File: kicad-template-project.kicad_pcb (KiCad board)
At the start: 4 copper layers, 1 part

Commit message: feat: initial layout
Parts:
- added C10: C, Capacitor_SMD:C_1206_3216Metric, B.Cu at (120.5, 145.0)
- added C11: C, Capacitor_SMD:C_1206_3216Metric, B.Cu at (118.0, 145.0)
- added C12: C, Capacitor_SMD:C_1206_3216Metric, B.Cu at (115.5, 145.0)
- added C13: C, Capacitor_SMD:C_1206_3216Metric, B.Cu at (132.5, 145.0)
- added C14: C, Capacitor_SMD:C_1206_3216Metric, B.Cu at (130.0, 145.0)
- added C15: C, Capacitor_SMD:C_1206_3216Metric, B.Cu at (127.5, 145.0)
- added C16: C, Capacitor_SMD:C_1206_3216Metric, B.Cu at (142.0, 145.0)
- added C19: C, Capacitor_SMD:C_1206_3216Metric, B.Cu at (139.5, 145.0)
- added C2: 100 nF, chenry-footprint-lib:C_0402, F.Cu at (141.0, 152.7)
- added C26: 100 nF, chenry-footprint-lib:C_0402, F.Cu at (117.0, 152.7)
- added C27: 100 nF, chenry-footprint-lib:C_0402, F.Cu at (129.0, 152.7)
- added C29: 100 nF, chenry-footprint-lib:C_0402, B.Cu at (117.8, 149.5)
- added C3: 100 nF, chenry-footprint-lib:C_0402, F.Cu at (122.0, 146.0)
- added C30: 100 nF, chenry-footprint-lib:C_0402, B.Cu at (129.8, 149.5)
- added C31: 100 nF, chenry-footprint-lib:C_0402, B.Cu at (141.8, 149.5)
- added C32: 100 nF, chenry-footprint-lib:C_0402, B.Cu at (116.8, 149.5)
- added C33: 100 nF, chenry-footprint-lib:C_0402, B.Cu at (128.8, 149.5)
- added C34: 100 nF, chenry-footprint-lib:C_0402, B.Cu at (140.8, 149.5)
- added C35: 100 nF, chenry-footprint-lib:C_0402, B.Cu at (115.8, 149.5)
- added C36: 100 nF, chenry-footprint-lib:C_0402, B.Cu at (127.8, 149.5)
- added C37: 100 nF, chenry-footprint-lib:C_0402, B.Cu at (139.8, 149.5)
- added C38: C, Capacitor_SMD:C_1206_3216Metric, B.Cu at (113.0, 145.0)
- added C39: C, Capacitor_SMD:C_1206_3216Metric, B.Cu at (125.0, 145.0)
- added C4: 100 nF, chenry-footprint-lib:C_0402, F.Cu at (113.5, 151.5)
- added C5: 100 nF, chenry-footprint-lib:C_0402, F.Cu at (134.0, 146.0)
- added C6: 100 nF, chenry-footprint-lib:C_0402, F.Cu at (125.5, 151.5)
- added C7: 100 nF, chenry-footprint-lib:C_0402, F.Cu at (137.5, 151.5)
- added C8: C, Capacitor_SMD:C_1206_3216Metric, B.Cu at (137.0, 145.0)
- added C9: C, Capacitor_SMD:C_1206_3216Metric, B.Cu at (144.5, 145.0)
- added H1: MountingHole_Pad, MountingHole:MountingHole_2.2mm_M2_DIN965_Pad, F.Cu at (138.0, 156.0)
- added H2: MountingHole_Pad, MountingHole:MountingHole_2.2mm_M2_DIN965_Pad, F.Cu at (120.5, 155.5)
- added H3: MountingHole_Pad, MountingHole:MountingHole_2.2mm_M2_DIN965_Pad, F.Cu at (129.0, 157.5)
- added J1: Conn_01x02_Pin, Connector_AMASS:AMASS_XT30PW-F_1x02_P2.50mm_Horizontal, F.Cu at (147.1, 132.8)
- added Q1: LMG2100R026, chenry-footprint-lib:VBN0018A-MFG, F.Cu at (140.5, 148.5)
- added Q2: LMG2100R026, chenry-footprint-lib:VBN0018A-MFG, F.Cu at (116.5, 148.5)
- added Q3: LMG2100R026, chenry-footprint-lib:VBN0018A-MFG, F.Cu at (128.5, 148.5)
- added R1: 10K, chenry-footprint-lib:R_0402, F.Cu at (147.0, 152.0)
- added R2: 10K, chenry-footprint-lib:R_0402, F.Cu at (123.0, 152.0)
- added R3: 10K, chenry-footprint-lib:R_0402, F.Cu at (135.0, 152.0)
- added U1: MCS1823, chenry-footprint-lib:MPS_MCS1823_TQFN-12_MNP, F.Cu at (145.8, 149.2)
- added U2: MCS1823, chenry-footprint-lib:MPS_MCS1823_TQFN-12_MNP, F.Cu at (121.8, 149.2)
- added U3: MCS1823, chenry-footprint-lib:MPS_MCS1823_TQFN-12_MNP, F.Cu at (133.8, 149.2)
- added U4: ICE40UP5K-SG48ITR, Package_DFN_QFN:QFN-48-1EP_7x7mm_P0.5mm_EP5.6x5.6mm, F.Cu at (112.0, 130.2)
- added U5: STM32G0B1RETx, Package_QFP:LQFP-64_10x10mm_P0.5mm, F.Cu at (121.8, 121.0)
- added U6: SN65HVD230, Package_SO:SOIC-8_3.9x4.9mm_P1.27mm, F.Cu at (133.8, 115.2)
- added U7: LAN8710A, Package_DFN_QFN:QFN-32-1EP_5x5mm_P0.5mm_EP3.3x3.3mm_ThermalVias, F.Cu at (133.8, 122.8)
- added U8: MLX90395xLW, Package_DFN_QFN:QFN-16-1EP_3x3mm_P0.5mm_EP1.675x1.675mm, B.Cu at (130.0, 135.0)
- C1: value 1 uF -> 100 nF
- moved C1 46.1 mm to (146.0, 146.0), turned to -90 degrees
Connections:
- C1 pad 1: unconnected-(C1-Pad1) -> GND
- C1 pad 2: unconnected-(C1-Pad2) -> VDD_3V3
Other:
- board outline added: 50 x 50 mm

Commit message: fix: adjusted positining
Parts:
- added U10: AD40xxBCPZ, Package_CSP:LFCSP-WD-10-1EP_3x3mm_P0.5mm_EP1.64x2.38mm, F.Cu at (128.8, 140.5)
- added U11: AD40xxBCPZ, Package_CSP:LFCSP-WD-10-1EP_3x3mm_P0.5mm_EP1.64x2.38mm, F.Cu at (140.5, 140.5)
- added U9: AD40xxBCPZ, Package_CSP:LFCSP-WD-10-1EP_3x3mm_P0.5mm_EP1.64x2.38mm, F.Cu at (116.8, 140.2)
- moved U4 1.00 mm to (112.0, 131.2)

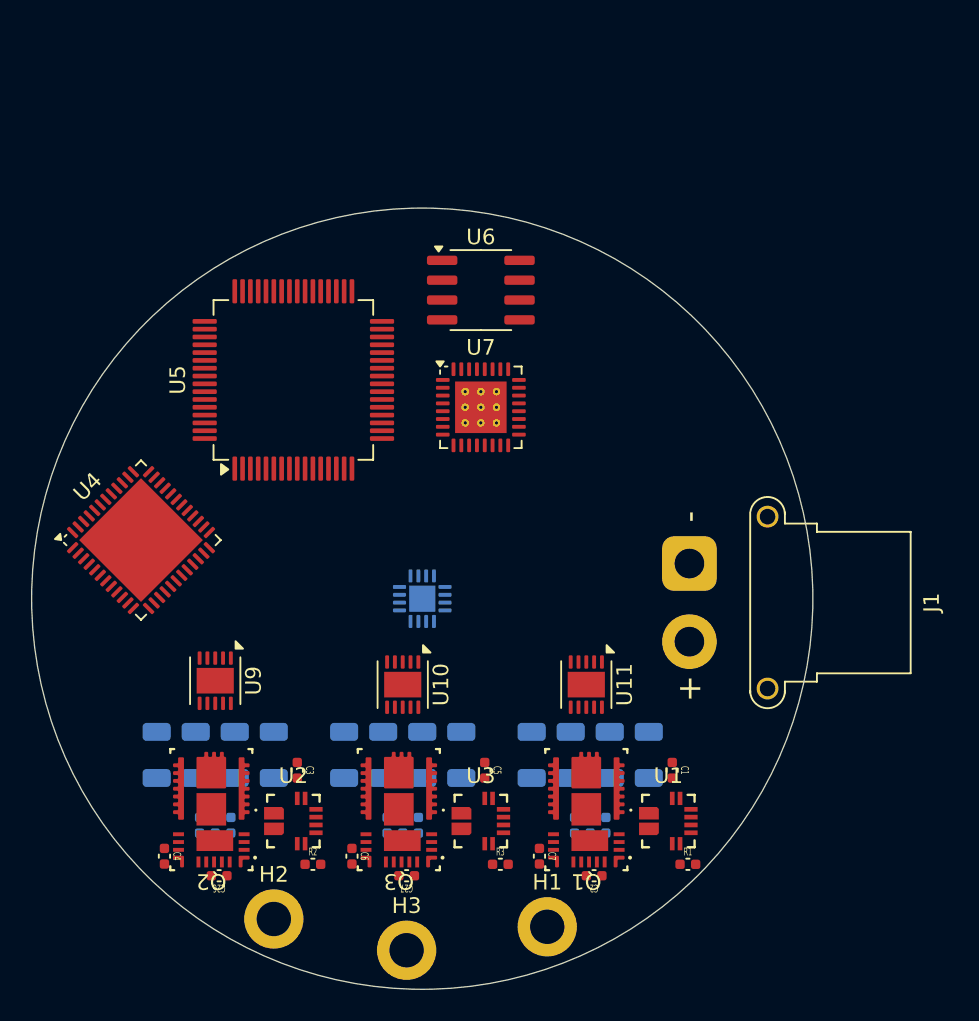
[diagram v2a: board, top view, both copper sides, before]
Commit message: fix: added switcher placeholders
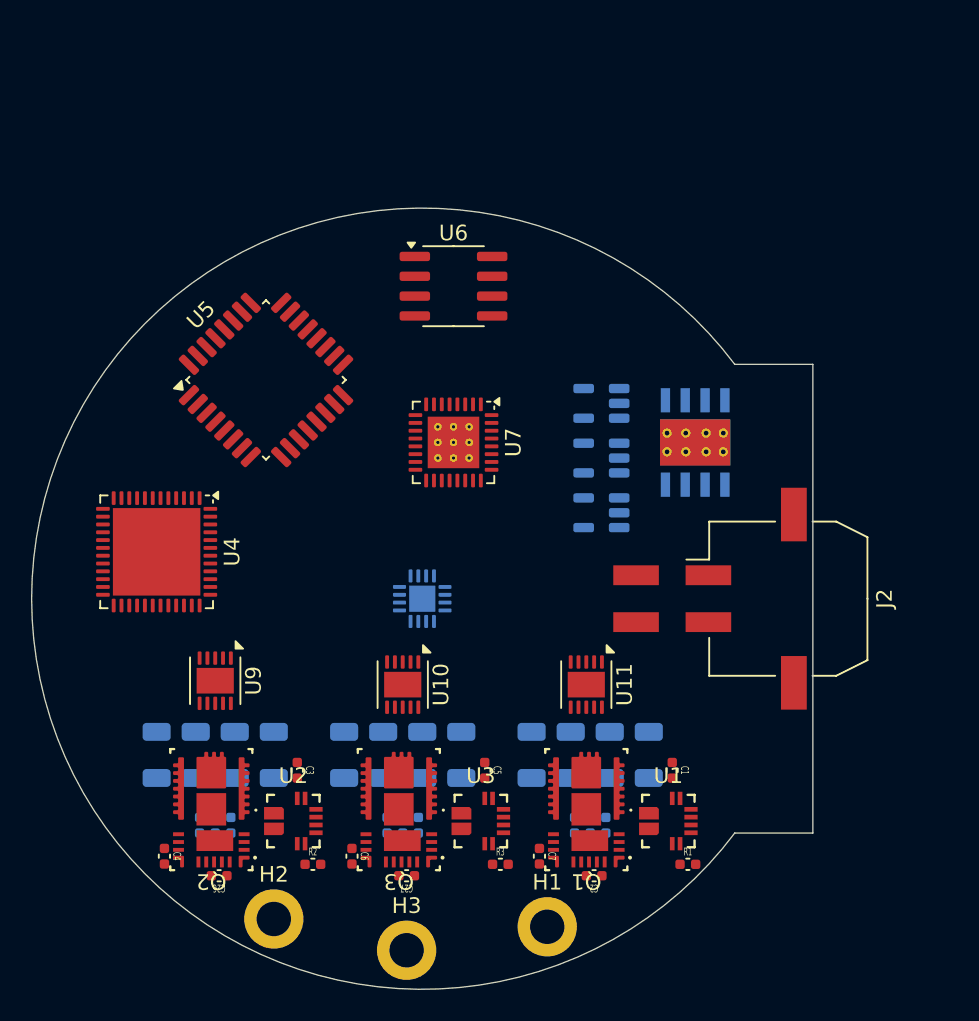
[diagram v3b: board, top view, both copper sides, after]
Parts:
- removed J1: Conn_01x02_Pin, Connector_AMASS:AMASS_XT30PW-F_1x02_P2.50mm_Horizontal
- added J2: Conn_01x04, Connector_Molex:Molex_Micro-Fit_3.0_43045-0410_2x02-1MP_P3.00mm_Horizontal, F.Cu at (146.0, 135.0)
- added U12: TPS54360DDA, Package_SO:TI_SO-PowerPAD-8_ThermalVias, B.Cu at (147.5, 125.0)
- added U13: MIC5219YM5, Package_TO_SOT_SMD:SOT-23-5, B.Cu at (141.5, 129.5)
- added U14: MIC5219YM5, Package_TO_SOT_SMD:SOT-23-5, B.Cu at (141.5, 122.5)
- added U15: MIC5219YM5, Package_TO_SOT_SMD:SOT-23-5, B.Cu at (141.5, 126.0)
- U5: value STM32G0B1RETx -> STM32G0B1KBTx; footprint Package_QFP:LQFP-64_10x10mm_P0.5mm -> Package_QFP:LQFP-32_7x7mm_P0.8mm
- moved U7 2.85 mm to (132.0, 125.0), turned to -90 degrees
- moved U6 1.77 mm to (132.0, 115.0)
- moved U5 1.75 mm to (120.0, 121.0), turned to 45 degrees
- moved U4 1.25 mm to (113.0, 132.0), turned to -90 degrees
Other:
- outline, holes or cut-outs redrawn

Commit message: feat: done rough board placements for general shape
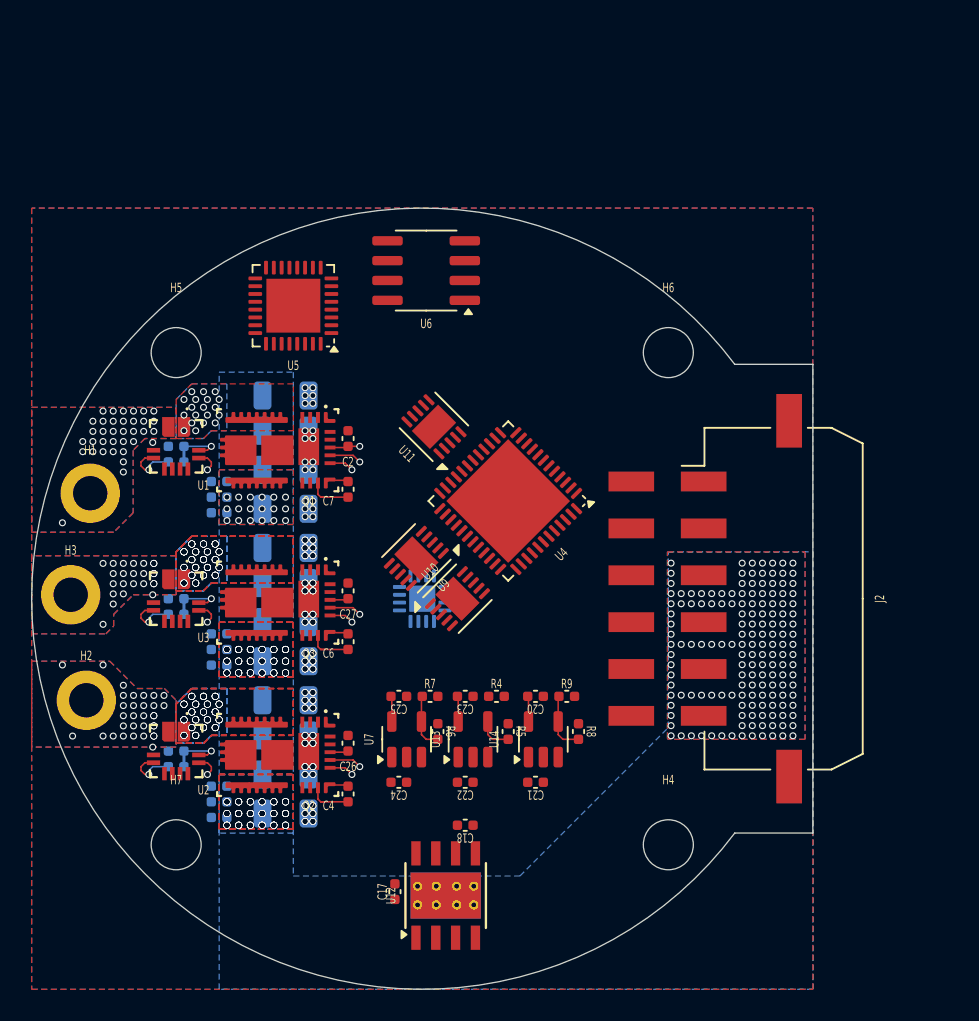
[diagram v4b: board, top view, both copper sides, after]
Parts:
- removed U15: MIC5219YM5, Package_TO_SOT_SMD:SOT-23-5
- added C17: 100 nF, chenry-footprint-lib:C_0402, F.Cu at (128.2, 153.8)
- added C18: 1 uF, chenry-footprint-lib:C_0402, F.Cu at (132.8, 149.5)
- added C20: 1 uF, chenry-footprint-lib:C_0402, F.Cu at (137.2, 141.3)
- added C21: 1 uF, chenry-footprint-lib:C_0402, F.Cu at (137.2, 146.8)
- added C22: 1 uF, chenry-footprint-lib:C_0402, F.Cu at (132.8, 146.8)
- added C23: 1 uF, chenry-footprint-lib:C_0402, F.Cu at (132.7, 141.3)
- added C24: 1 uF, chenry-footprint-lib:C_0402, F.Cu at (128.5, 146.8)
- added C25: 1 uF, chenry-footprint-lib:C_0402, F.Cu at (128.5, 141.3)
- added H4: MountingHole, MountingHole:MountingHole_3.2mm_M3, F.Cu at (145.8, 150.8)
- added H5: MountingHole, MountingHole:MountingHole_3.2mm_M3, F.Cu at (114.2, 119.2)
- added H6: MountingHole, MountingHole:MountingHole_3.2mm_M3, F.Cu at (145.8, 119.2)
- added H7: MountingHole, MountingHole:MountingHole_3.2mm_M3, F.Cu at (114.2, 150.8)
- added R4: 10K, chenry-footprint-lib:R_0402, F.Cu at (134.8, 141.3)
- added R5: 10K, chenry-footprint-lib:R_0402, F.Cu at (135.5, 143.5)
- added R6: 10K, chenry-footprint-lib:R_0402, F.Cu at (131.0, 143.5)
- added R7: 10K, chenry-footprint-lib:R_0402, F.Cu at (130.5, 141.3)
- added R8: 10K, chenry-footprint-lib:R_0402, F.Cu at (140.0, 143.5)
- added R9: 10K, chenry-footprint-lib:R_0402, F.Cu at (139.2, 141.3)
- C1, C3, C5, R1, R2, R3: moved to B.Cu
- J2: value Conn_01x04 -> Conn_01x12; footprint Connector_Molex:Molex_Micro-Fit_3.0_43045-0410_2x02-1MP_P3.00mm_Horizontal -> Connector_Molex:Molex_Micro-Fit_3.0_43045-1210_2x06-1MP_P3.00mm_Horizontal
- U12, U13, U14: moved to F.Cu
- U5: value STM32G0B1KBTx -> STM32L432KBUx; footprint Package_QFP:LQFP-32_7x7mm_P0.8mm -> Package_DFN_QFN:QFN-32-1EP_5x5mm_P0.5mm_EP3.45x3.45mm
- U7: value LAN8710A -> MIC5219YM5; footprint Package_DFN_QFN:QFN-32-1EP_5x5mm_P0.5mm_EP3.3x3.3mm_ThermalVias -> Package_TO_SOT_SMD:SOT-23-5
- moved R1 41.7 mm to (114.2, 126.2)
- moved H1 40.3 mm to (108.8, 128.2)
- moved U1 39.6 mm to (114.2, 125.2), turned to -90 degrees
- moved C1 37.9 mm to (114.2, 125.2), turned to 0 degrees
- moved U12 33.1 mm to (131.5, 154.0), turned to 90 degrees
- moved C9 32.7 mm to (121.2, 122.0), turned to 0 degrees
- moved C2 32.1 mm to (125.2, 124.8), turned to -90 degrees
- moved C31 31.8 mm to (117.0, 129.5), turned to 180 degrees
- moved C34 31.7 mm to (117.0, 128.5), turned to 180 degrees
- moved C37 31.6 mm to (117.0, 127.5), turned to 180 degrees
- moved H3 31.3 mm to (107.5, 134.8)
- moved Q1 30.3 mm to (120.8, 125.5), turned to -90 degrees
- moved C16 29.3 mm to (121.2, 124.2), turned to 0 degrees
- moved C7 26.5 mm to (125.2, 128.0), turned to 90 degrees
- moved R3 26.2 mm to (114.2, 136.0)
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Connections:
- J2 pad 3: unconnected-(J2-Pin_3-Pad3) -> VDD_48V
- J2 pad 4: unconnected-(J2-Pin_4-Pad4) -> VDD_48V
- U12 pad 1: unconnected-(U12-BOOT-Pad1) -> Net-(U12-BOOT)
- U12 pad 2: unconnected-(U12-VIN-Pad2) -> VDD_48V
- U12 pad 7: unconnected-(U12-GND-Pad7) -> GND
- U12 pad 8: unconnected-(U12-SW-Pad8) -> Net-(D1-K)
- U12 pad 9: unconnected-(U12-GNDPAD-Pad9) -> GND
- U13 pad 1: unconnected-(U13-IN-Pad1) -> VDD_6V
- U13 pad 2: unconnected-(U13-GND-Pad2) -> GND
- U13 pad 3: unconnected-(U13-EN-Pad3) -> VDD_6V
- U13 pad 4: unconnected-(U13-ADJ-Pad4) -> Net-(U13-ADJ)
- U13 pad 5: unconnected-(U13-OUT-Pad5) -> VDD_5V
- U14 pad 1: unconnected-(U14-IN-Pad1) -> VDD_6V
- U14 pad 2: unconnected-(U14-GND-Pad2) -> GND
- U14 pad 3: unconnected-(U14-EN-Pad3) -> VDD_6V
- U14 pad 4: unconnected-(U14-ADJ-Pad4) -> Net-(U14-ADJ)
- U14 pad 5: unconnected-(U14-OUT-Pad5) -> VDD_2V5
- U5 pad 1: unconnected-(U5-PB9-Pad1) -> VDD_3V3
- U5 pad 16: unconnected-(U5-PB1-Pad16) -> GND
- U5 pad 17: unconnected-(U5-PB2-Pad17) -> VDD_3V3
- U5 pad 32: unconnected-(U5-PB8-Pad32) -> GND
- U5 pad 5: unconnected-(U5-VSS-Pad5) -> VDD_3V3
- U7 pad 1: unconnected-(U7-VDD2A-Pad1) -> VDD_6V
- U7 pad 2: unconnected-(U7-LED2/~{INTSEL}-Pad2) -> GND
- U7 pad 3: unconnected-(U7-LED1/~{REGOFF}-Pad3) -> VDD_6V
- U7 pad 4: unconnected-(U7-XTAL2-Pad4) -> Net-(U7-ADJ)
- U7 pad 5: unconnected-(U7-XTAL1/CLKIN-Pad5) -> VDD_3V3
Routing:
- net VDD_3V3: track 0.00 -> 12.6 mm, vias 0 -> 3
- net VDD_5V: track 0.00 -> 5.93 mm, vias 0 -> 1
- net Net-(U14-ADJ): track 0.00 -> 3.89 mm
- net Net-(U7-ADJ): track 0.00 -> 3.64 mm
- net /PH2/ISNS: track 0.00 -> 3.52 mm, vias 0 -> 1
- net /PH1/ISNS: track 0.00 -> 3.52 mm, vias 0 -> 1
- net /PH0/ISNS: track 0.00 -> 3.52 mm, vias 0 -> 1
- net /PH2/I_OCD: track 0.00 -> 3.31 mm, vias 0 -> 1
- net /PH1/I_OCD: track 0.00 -> 3.31 mm, vias 0 -> 1
- net /PH0/I_OCD: track 0.00 -> 3.31 mm, vias 0 -> 1
- net Net-(Q3-HB): track 0.00 -> 2.97 mm
- net Net-(Q2-HB): track 0.00 -> 2.97 mm
- net Net-(Q1-HB): track 0.00 -> 2.97 mm
- net Net-(U13-ADJ): track 0.00 -> 2.26 mm
- net /PH2/PWM_LI: track 0.00 -> 2.08 mm, vias 0 -> 1
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- added copper zone on B.Cu, net /PH0/HB_SW
- added copper zone on F.Cu, net /PH0/HB_SW
- added copper zone on In2.Cu, net /PH0/HB_SW
- added copper zone on In3.Cu, net /PH0/HB_SW
- added copper zone on In4.Cu, net /PH0/HB_SW
- added copper zone on B.Cu, net /PH0/PH_OUT
- added copper zone on F.Cu, net /PH0/PH_OUT
- added copper zone on In1.Cu, net /PH0/PH_OUT
- added copper zone on In2.Cu, net /PH0/PH_OUT
- added copper zone on In3.Cu, net /PH0/PH_OUT
- added copper zone on In4.Cu, net /PH0/PH_OUT
- added copper zone on B.Cu, net /PH1/HB_SW
- added copper zone on F.Cu, net /PH1/HB_SW
- added copper zone on In2.Cu, net /PH1/HB_SW
- added copper zone on In3.Cu, net /PH1/HB_SW
- added copper zone on In4.Cu, net /PH1/HB_SW
- added copper zone on B.Cu, net /PH1/PH_OUT
- added copper zone on F.Cu, net /PH1/PH_OUT
- added copper zone on In1.Cu, net /PH1/PH_OUT
- added copper zone on In2.Cu, net /PH1/PH_OUT
- added copper zone on In3.Cu, net /PH1/PH_OUT
- added copper zone on In4.Cu, net /PH1/PH_OUT
- added copper zone on B.Cu, net /PH2/HB_SW
- added copper zone on F.Cu, net /PH2/HB_SW
- added copper zone on In2.Cu, net /PH2/HB_SW
- added copper zone on In3.Cu, net /PH2/HB_SW
- added copper zone on In4.Cu, net /PH2/HB_SW
- added copper zone on B.Cu, net /PH2/PH_OUT
- added copper zone on F.Cu, net /PH2/PH_OUT
- added copper zone on In1.Cu, net /PH2/PH_OUT
- added copper zone on In2.Cu, net /PH2/PH_OUT
- added copper zone on In3.Cu, net /PH2/PH_OUT
- added copper zone on In4.Cu, net /PH2/PH_OUT
- added copper zone on B.Cu, net GND
- added copper zone on F.Cu, net GND
- added copper zone on In1.Cu, net GND
- added copper zone on In3.Cu, net GND
- added copper zone on In2.Cu, net VDD_3V3
- added copper zone on In4.Cu, net VDD_3V3
- added copper zone on B.Cu, net VDD_48V
- added copper zone on F.Cu, net VDD_48V
- added copper zone on In1.Cu, net VDD_48V
- added copper zone on In2.Cu, net VDD_48V
- added copper zone on In3.Cu, net VDD_48V
- added copper zone on In4.Cu, net VDD_48V
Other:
- copper layers 4 -> 6
